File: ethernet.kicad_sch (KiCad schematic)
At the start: 45 parts, among them J401 Bus_RJ45_5-2337992-8, Q401 PJE138K, U401 TPS2372-3RGWR, U402 ACPL-217-500E, U403 ULS-12/5-D48N-C

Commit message: [#53901] Update symbols & footprints from lib
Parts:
- D404: footprint antmicro-footprints:LED_0603_1608Metric_R -> antmicro-footprints:LED_0603_1608Metric_G; symbol antmicroLEDIndicationDiscrete:LED_R_0603_598-8D80-107F -> antmicroLEDIndicationDiscrete:LED_G_0603_598-8D80-107F
- R407, R409, R410, R417, R419, R420, R422, R423: DNP DNP -> (none); now in the parts list
- U403: value ULS-12/5-D48N-C -> ULS-12_5-D48N-C; symbol antmicroDCDCConverters:ULS-12/5-D48N-C -> antmicroDCDCConverters:ULS-12_5-D48N-C

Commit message: [#56708] Add loclib
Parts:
- C401: footprint antmicro-footprints:C_0805_2012Metric -> cm4-baseboard-footprints:C_0805_2012Metric; symbol antmicroCapacitorsmisc:C_100n_100V_0805 -> cm4-baseboard:C_100n_100V_0805
- C402: footprint antmicro-footprints:C_0402_1005Metric -> cm4-baseboard-footprints:C_0402_1005Metric; symbol antmicroCapacitors0402:C_10n_0402 -> cm4-baseboard:C_10n_0402
- C403, C411: footprint antmicro-footprints:C_0402_1005Metric -> cm4-baseboard-footprints:C_0402_1005Metric; symbol antmicroCapacitors0402:C_100n_0402 -> cm4-baseboard:C_100n_0402
- C404, C405, C406, C407: footprint antmicro-footprints:C_2220_5650Metric -> cm4-baseboard-footprints:C_2220_5650Metric; symbol antmicroCapacitorsmisc:C_22u_100V_2220 -> cm4-baseboard:C_22u_100V_2220
- C408, C409, C410: footprint antmicro-footprints:C_0805_2012Metric -> cm4-baseboard-footprints:C_0805_2012Metric; symbol antmicroCapacitorsmisc:C_22u_25V_0805 -> cm4-baseboard:C_22u_25V_0805
- D401, D402: footprint antmicro-footprints:DFN3538 -> cm4-baseboard-footprints:DFN3538; symbol antmicroTVSDiodes:CD-MMBL110S -> cm4-baseboard:CD-MMBL110S
- D403: footprint antmicro-footprints:D_SOD-123F -> cm4-baseboard-footprints:D_SOD-123F; symbol antmicroDiodesRectifiersSingle:PTVS58VS1UR,115 -> cm4-baseboard:PTVS58VS1UR,115
- D404: footprint antmicro-footprints:LED_0603_1608Metric_G -> cm4-baseboard-footprints:LED_0603_1608Metric_G; symbol antmicroLEDIndicationDiscrete:LED_G_0603_598-8D80-107F -> cm4-baseboard:LED_G_0603_598-8D80-107F
- FB401, FB402: footprint antmicro-footprints:FB_0603_1608Metric -> cm4-baseboard-footprints:FB_0603_1608Metric; symbol antmicroFerriteBeadsandChips:FB_220Z_2.2A_TDK-MPZ_0603 -> cm4-baseboard:FB_220Z_2.2A_TDK-MPZ_0603
- J401: footprint antmicro-footprints:RJ45_5-2337992-8_Horizontal -> cm4-baseboard-footprints:RJ45_5-2337992-8_Horizontal; symbol antmicroModularConnectorsJacksWithMagnetics:Bus_RJ45_5-2337992-8 -> cm4-baseboard:Bus_RJ45_5-2337992-8
- Q401: footprint antmicro-footprints:SOT-523 -> cm4-baseboard-footprints:SOT-523; symbol antmicroTransistorsFETsMOSFETsSingle:PJE138K -> cm4-baseboard:PJE138K
- R401: footprint antmicro-footprints:R_0402_1005Metric -> cm4-baseboard-footprints:R_0402_1005Metric; symbol antmicroResistors0402:R_1k3_0402 -> cm4-baseboard:R_1k3_0402
- R402: footprint antmicro-footprints:R_0402_1005Metric -> cm4-baseboard-footprints:R_0402_1005Metric; symbol antmicroResistors0402:R_49k9_0402 -> cm4-baseboard:R_49k9_0402
- R403, R417, R422, R423: footprint antmicro-footprints:R_0402_1005Metric -> cm4-baseboard-footprints:R_0402_1005Metric; symbol antmicroResistors0402:R_0R_0402 -> cm4-baseboard:R_0R_0402
- R404: footprint antmicro-footprints:R_0603_1608Metric -> cm4-baseboard-footprints:R_0603_1608Metric; symbol antmicroResistors0603:R_63R4_0603 -> cm4-baseboard:R_63R4_0603
- R405: footprint antmicro-footprints:R_0402_1005Metric -> cm4-baseboard-footprints:R_0402_1005Metric; symbol antmicroResistors0402:R_1k2_0402 -> cm4-baseboard:R_1k2_0402
- R406, R414: footprint antmicro-footprints:R_0402_1005Metric -> cm4-baseboard-footprints:R_0402_1005Metric; symbol antmicroResistors0402:R_24k9_0402 -> cm4-baseboard:R_24k9_0402
- R407, R408, R409, R410: footprint antmicro-footprints:R_0402_1005Metric -> cm4-baseboard-footprints:R_0402_1005Metric; symbol antmicroResistors0402:R_10k_0402 -> cm4-baseboard:R_10k_0402
- R411, R412, R413: footprint antmicro-footprints:R_0402_1005Metric -> cm4-baseboard-footprints:R_0402_1005Metric; symbol antmicroResistors0402:R_200R_0402 -> cm4-baseboard:R_200R_0402
- R415, R419: footprint antmicro-footprints:R_0402_1005Metric -> cm4-baseboard-footprints:R_0402_1005Metric; symbol antmicroResistors0402:R_470k_0402 -> cm4-baseboard:R_470k_0402
- R416, R420: footprint antmicro-footprints:R_0402_1005Metric -> cm4-baseboard-footprints:R_0402_1005Metric; symbol antmicroResistors0402:R_100k_0402 -> cm4-baseboard:R_100k_0402
- R418, R421: footprint antmicro-footprints:R_0402_1005Metric -> cm4-baseboard-footprints:R_0402_1005Metric; symbol antmicroResistors0402:R_1k_0402 -> cm4-baseboard:R_1k_0402
- U401: footprint antmicro-footprints:VQFN-20_5x5x1mm_P0.65mm -> cm4-baseboard-footprints:VQFN-20_5x5x1mm_P0.65mm; symbol antmicroPMICPowerDistributionSwitchesLoadDrivers:TPS2372-3RGWR -> cm4-baseboard:TPS2372-3RGWR
- U402: footprint antmicro-footprints:SOIC-4_4.55x2.6mm_P1.27mm -> cm4-baseboard-footprints:SOIC-4_4.55x2.6mm_P1.27mm; symbol antmicroOptoisolatorsLogicOutput:ACPL-217-500E -> cm4-baseboard:ACPL-217-500E
- U403: footprint antmicro-footprints:ULS-12_5-D48N-C -> cm4-baseboard-footprints:ULS-12_5-D48N-C; symbol antmicroDCDCConverters:ULS-12_5-D48N-C -> cm4-baseboard:ULS-12_5-D48N-C

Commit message: [#56708] Update symbol/footprint props; Update modules visibilty
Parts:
- D404: value LED_G -> LED_G_0603_598-8D80-107F; Color (none) -> Green
- R407, R409, R410, R417, R419, R420, R422, R423: DNP (none) -> DNP; now left out of the parts list
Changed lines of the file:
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@@
   )
   (symbol (lib_id "cm4-baseboard:R_0R_0402") (at 331.47 191.77 270) (unit 1)
-    (in_bom yes) (on_board yes) (dnp yes)
+    (in_bom no) (on_board yes) (dnp yes)
     (property "Reference" "R423" (at 332.74 193.04 90)
       (effects (font (size 1.27 1.27)) (justify left))
@@
     (property "Current" "1A" (at 330.2 191.135 0)
       (effects (font (size 1.27 1.27) (thickness 0.15)) hide)
+    )
+    (property "DNP" "DNP" (at 331.47 194.31 0)
+      (effects (font (size 1 1)))
     )
     (pin "1")
@@
   )
   (symbol (lib_id "cm4-baseboard:R_0R_0402") (at 274.32 194.31 180) (unit 1)
-    (in_bom yes) (on_board yes) (dnp yes)
+    (in_bom no) (on_board yes) (dnp yes)
     (property "Reference" "R417" (at 271.78 190.5 0)
       (effects (font (size 1.27 1.27)))
@@
       (effects (font (size 1.27 1.27) (thickness 0.15)) hide)
     )
+    (property "DNP" "DNP" (at 271.78 194.31 0)
+      (effects (font (size 1 1)))
+    )
     (pin "1")
     (pin "2")
@@
       (effects (font (size 1.27 1.27) (thickness 0.15)) (justify left))
     )
-    (property "Value" "LED_G" (at 252.73 198.4375 90)
-      (effects (font (size 1.27 1.27) (thickness 0.15)) (justify left))
-    )
-    (property "Footprint" "cm4-baseboard-footprints:LED_0603_1608Metric_G" (at 240.03 215.9 0)
-      (effects (font (size 1.27 1.27) (thickness 0.15)) (justify left bottom) hide)
-    )
-    (property "Datasheet" "https://www.farnell.com/datasheets/3093797.pdf" (at 237.49 215.9 0)
-      (effects (font (size 1.27 1.27) (thickness 0.15)) (justify left bottom) hide)
-    )
-    (property "MPN" "598-8D80-107F" (at 234.95 215.9 0)
-      (effects (font (size 1.27 1.27) (thickness 0.15)) (justify left bottom) hide)
-    )
-    (property "Manufacturer" "Dialight" (at 232.41 215.9 0)
-      (effects (font (size 1.27 1.27) (thickness 0.15)) (justify left bottom) hide)
-    )
-    (property "Author" "Antmicro" (at 229.87 215.9 0)
-      (effects (font (size 1.27 1.27) (thickness 0.15)) (justify left bottom) hide)
-    )
-    (property "License" "Apache-2.0" (at 227.33 215.9 0)
-      (effects (font (size 1.27 1.27) (thickness 0.15)) (justify left bottom) hide)
+    (property "Value" "LED_G_0603_598-8D80-107F" (at 240.03 215.9 0)
+      (effects (font (size 1.27 1.27) (thickness 0.15)) (justify left bottom) hide)
+    )
+    (property "Footprint" "cm4-baseboard-footprints:LED_0603_1608Metric_G" (at 237.49 215.9 0)
+      (effects (font (size 1.27 1.27) (thickness 0.15)) (justify left bottom) hide)
+    )
+    (property "Datasheet" "https://www.farnell.com/datasheets/3093797.pdf" (at 234.95 215.9 0)
+      (effects (font (size 1.27 1.27) (thickness 0.15)) (justify left bottom) hide)
+    )
+    (property "MPN" "598-8D80-107F" (at 232.41 215.9 0)
+      (effects (font (size 1.27 1.27) (thickness 0.15)) (justify left bottom) hide)
+    )
+    (property "Manufacturer" "Dialight" (at 229.87 215.9 0)
+      (effects (font (size 1.27 1.27) (thickness 0.15)) (justify left bottom) hide)
+    )
+    (property "Author" "Antmicro" (at 227.33 215.9 0)
+      (effects (font (size 1.27 1.27) (thickness 0.15)) (justify left bottom) hide)
+    )
+    (property "License" "Apache-2.0" (at 224.79 215.9 0)
+      (effects (font (size 1.27 1.27) (thickness 0.15)) (justify left bottom) hide)
+    )
+    (property "Color" "Green" (at 252.73 198.4375 90)
+      (effects (font (size 1.27 1.27)) (justify left))
     )
     (pin "1")
@@
   (symbol (lib_id "cm4-baseboard:FB_220Z_2.2A_TDK-MPZ_0603") (at 97.79 213.36 0) (unit 1)
     (in_bom yes) (on_board yes) (dnp no) (fields_autoplaced)
-    (property "Reference" "FB402" (at 100.2919 217.17 0)
+    (property "Reference" "FB402" (at 100.2919 207.01 0)
       (effects (font (size 1.27 1.27)))
     )
@@
       (effects (font (size 1.27 1.27) (thickness 0.15)) (justify left bottom) hide)
     )
-    (property "Val" "220Z/2.2A" (at 0 426.72 0)
+    (property "Val" "220Z/2.2A" (at 100.2919 209.55 0)
       (effects (font (size 1.27 1.27)))
     )
@@
   )
   (symbol (lib_id "cm4-baseboard:R_470k_0402") (at 287.02 189.23 90) (unit 1)
-    (in_bom yes) (on_board yes) (dnp yes)
+    (in_bom no) (on_board yes) (dnp yes)
     (property "Reference" "R419" (at 288.29 185.42 90)
       (effects (font (size 1.27 1.27)) (justify right))
@@
       (effects (font (size 1.27 1.27)) (justify left bottom) hide)
     )
+    (property "DNP" "DNP" (at 287.02 186.69 0)
+      (effects (font (size 1 1)))
+    )
     (pin "1")
     (pin "2")
@@
   )
   (symbol (lib_id "cm4-baseboard:R_100k_0402") (at 287.02 203.2 90) (unit 1)
-    (in_bom yes) (on_board yes) (dnp yes)
+    (in_bom no) (on_board yes) (dnp yes)
     (property "Reference" "R420" (at 288.29 199.39 90)
       (effects (font (size 1.27 1.27)) (justify right))
@@
       (effects (font (size 1.27 1.27)) (justify left bottom) hide)
     )
+    (property "DNP" "DNP" (at 287.02 200.66 0)
+      (effects (font (size 1 1)))
+    )
     (pin "1")
     (pin "2")
@@
   )
   (symbol (lib_id "cm4-baseboard:R_0R_0402") (at 331.47 184.15 270) (unit 1)
-    (in_bom yes) (on_board yes) (dnp yes)
+    (in_bom no) (on_board yes) (dnp yes)
     (property "Reference" "R422" (at 332.74 185.42 90)
       (effects (font (size 1.27 1.27)) (justify left))
@@
     (property "Current" "1A" (at 330.2 183.515 0)
       (effects (font (size 1.27 1.27) (thickness 0.15)) hide)
+    )
+    (property "DNP" "DNP" (at 331.47 186.69 0)
+      (effects (font (size 1 1)))
     )
     (pin "1")
@@
   )
   (symbol (lib_id "cm4-baseboard:R_10k_0402") (at 185.42 189.23 90) (unit 1)
-    (in_bom yes) (on_board yes) (dnp yes) (fields_autoplaced)
+    (in_bom no) (on_board yes) (dnp yes)
     (property "Reference" "R407" (at 186.69 186.055 90)
       (effects (font (size 1.27 1.27)) (justify right))
@@
       (effects (font (size 1.27 1.27)) (justify left bottom) hide)
     )
+    (property "DNP" "DNP" (at 185.42 186.69 0)
+      (effects (font (size 1 1)))
+    )
     (pin "1")
     (pin "2")
@@
       (effects (font (size 1.27 1.27) (thickness 0.15)) (justify left bottom) hide)
     )
-    (property "Val" "220Z/2.2A" (at 0 365.76 0)
+    (property "Val" "220Z/2.2A" (at 100.2919 179.07 0)
       (effects (font (size 1.27 1.27)))
     )
@@
   )
   (symbol (lib_id "cm4-baseboard:R_10k_0402") (at 195.58 189.23 90) (unit 1)
-    (in_bom yes) (on_board yes) (dnp yes)
+    (in_bom no) (on_board yes) (dnp yes)
     (property "Reference" "R409" (at 196.85 186.055 90)
       (effects (font (size 1.27 1.27)) (justify right))
@@
       (effects (font (size 1.27 1.27)) (justify left bottom) hide)
     )
+    (property "DNP" "DNP" (at 195.58 186.69 0)
+      (effects (font (size 1 1)))
+    )
     (pin "1")
     (pin "2")
@@
   )
   (symbol (lib_id "cm4-baseboard:R_10k_0402") (at 204.47 189.23 90) (unit 1)
-    (in_bom yes) (on_board yes) (dnp yes)
+    (in_bom no) (on_board yes) (dnp yes)
     (property "Reference" "R410" (at 205.74 186.055 90)
       (effects (font (size 1.27 1.27)) (justify right))
@@
       (effects (font (size 1.27 1.27)) (justify left bottom) hide)
     )
-    (pin "1")
+    (property "DNP" "DNP" (at 204.47 186.69 0)
+      (effects (font (size 1 1)))
+    )
+    (pin "1")

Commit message: [#57456] Remove loclib
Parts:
- C401: footprint cm4-baseboard-footprints:C_0805_2012Metric -> antmicro-footprints:C_0805_2012Metric; symbol cm4-baseboard:C_100n_100V_0805 -> antmicroCapacitorsmisc:C_100n_100V_0805
- C402: footprint cm4-baseboard-footprints:C_0402_1005Metric -> antmicro-footprints:C_0402_1005Metric; symbol cm4-baseboard:C_10n_0402 -> antmicroCapacitors0402:C_10n_0402
- C403, C411: footprint cm4-baseboard-footprints:C_0402_1005Metric -> antmicro-footprints:C_0402_1005Metric; symbol cm4-baseboard:C_100n_0402 -> antmicroCapacitors0402:C_100n_0402
- C404, C405, C406, C407: footprint cm4-baseboard-footprints:C_2220_5650Metric -> antmicro-footprints:C_2220_5650Metric; symbol cm4-baseboard:C_22u_100V_2220 -> antmicroCapacitorsmisc:C_22u_100V_2220
- C408, C409, C410: footprint cm4-baseboard-footprints:C_0805_2012Metric -> antmicro-footprints:C_0805_2012Metric; symbol cm4-baseboard:C_22u_25V_0805 -> antmicroCapacitorsmisc:C_22u_25V_0805
- D401, D402: footprint cm4-baseboard-footprints:DFN3538 -> antmicro-footprints:DFN3538; symbol cm4-baseboard:CD-MMBL110S -> antmicroTVSDiodes:CD-MMBL110S
- D403: footprint cm4-baseboard-footprints:D_SOD-123F -> antmicro-footprints:D_SOD-123F; symbol cm4-baseboard:PTVS58VS1UR,115 -> antmicroDiodesRectifiersSingle:PTVS58VS1UR,115
- D404: footprint cm4-baseboard-footprints:LED_0603_1608Metric_G -> antmicro-footprints:LED_0603_1608Metric_G; symbol cm4-baseboard:LED_G_0603_598-8D80-107F -> antmicroLEDIndicationDiscrete:LED_G_0603_598-8D80-107F
- FB401, FB402: footprint cm4-baseboard-footprints:FB_0603_1608Metric -> antmicro-footprints:FB_0603_1608Metric; symbol cm4-baseboard:FB_220Z_2.2A_TDK-MPZ_0603 -> antmicroFerriteBeadsandChips:FB_220Z_2.2A_TDK-MPZ_0603
- J401: footprint cm4-baseboard-footprints:RJ45_5-2337992-8_Horizontal -> antmicro-footprints:RJ45_X-2337992-8_Horizontal; symbol cm4-baseboard:Bus_RJ45_5-2337992-8 -> antmicroModularConnectorsJacksWithMagnetics:Bus_RJ45_5-2337992-8
- Q401: footprint cm4-baseboard-footprints:SOT-523 -> antmicro-footprints:SOT-523; symbol cm4-baseboard:PJE138K -> antmicroTransistorsFETsMOSFETsSingle:PJE138K
- R401: footprint cm4-baseboard-footprints:R_0402_1005Metric -> antmicro-footprints:R_0402_1005Metric; symbol cm4-baseboard:R_1k3_0402 -> antmicroResistors0402:R_1k3_0402
- R402: footprint cm4-baseboard-footprints:R_0402_1005Metric -> antmicro-footprints:R_0402_1005Metric; symbol cm4-baseboard:R_49k9_0402 -> antmicroResistors0402:R_49k9_0402
- R403, R417, R422, R423: footprint cm4-baseboard-footprints:R_0402_1005Metric -> antmicro-footprints:R_0402_1005Metric; symbol cm4-baseboard:R_0R_0402 -> antmicroResistors0402:R_0R_0402
- R404: footprint cm4-baseboard-footprints:R_0603_1608Metric -> antmicro-footprints:R_0603_1608Metric; symbol cm4-baseboard:R_63R4_0603 -> antmicroResistors0603:R_63R4_0603
- R405: footprint cm4-baseboard-footprints:R_0402_1005Metric -> antmicro-footprints:R_0402_1005Metric; symbol cm4-baseboard:R_1k2_0402 -> antmicroResistors0402:R_1k2_0402
- R406, R414: footprint cm4-baseboard-footprints:R_0402_1005Metric -> antmicro-footprints:R_0402_1005Metric; symbol cm4-baseboard:R_24k9_0402 -> antmicroResistors0402:R_24k9_0402
- R407, R408, R409, R410: footprint cm4-baseboard-footprints:R_0402_1005Metric -> antmicro-footprints:R_0402_1005Metric; symbol cm4-baseboard:R_10k_0402 -> antmicroResistors0402:R_10k_0402
- R411, R412, R413: footprint cm4-baseboard-footprints:R_0402_1005Metric -> antmicro-footprints:R_0402_1005Metric; symbol cm4-baseboard:R_200R_0402 -> antmicroResistors0402:R_200R_0402
- R415, R419: footprint cm4-baseboard-footprints:R_0402_1005Metric -> antmicro-footprints:R_0402_1005Metric; symbol cm4-baseboard:R_470k_0402 -> antmicroResistors0402:R_470k_0402
- R416, R420: footprint cm4-baseboard-footprints:R_0402_1005Metric -> antmicro-footprints:R_0402_1005Metric; symbol cm4-baseboard:R_100k_0402 -> antmicroResistors0402:R_100k_0402
- R418, R421: footprint cm4-baseboard-footprints:R_0402_1005Metric -> antmicro-footprints:R_0402_1005Metric; symbol cm4-baseboard:R_1k_0402 -> antmicroResistors0402:R_1k_0402
- U401: footprint cm4-baseboard-footprints:VQFN-20_5x5x1mm_P0.65mm -> antmicro-footprints:VQFN-20_5x5x1mm_P0.65mm; symbol cm4-baseboard:TPS2372-3RGWR -> antmicroPMICPowerDistributionSwitchesLoadDrivers:TPS2372-3RGWR
- U402: footprint cm4-baseboard-footprints:SOIC-4_4.55x2.6mm_P1.27mm -> antmicro-footprints:SOIC-4_4.55x2.6mm_P1.27mm; symbol cm4-baseboard:ACPL-217-500E -> antmicroOptoisolatorsLogicOutput:ACPL-217-500E
- U403: footprint cm4-baseboard-footprints:ULS-12_5-D48N-C -> antmicro-footprints:ULS-12_5-D48N-C; symbol cm4-baseboard:ULS-12_5-D48N-C -> antmicroDCDCConverters:ULS-12_5-D48N-C

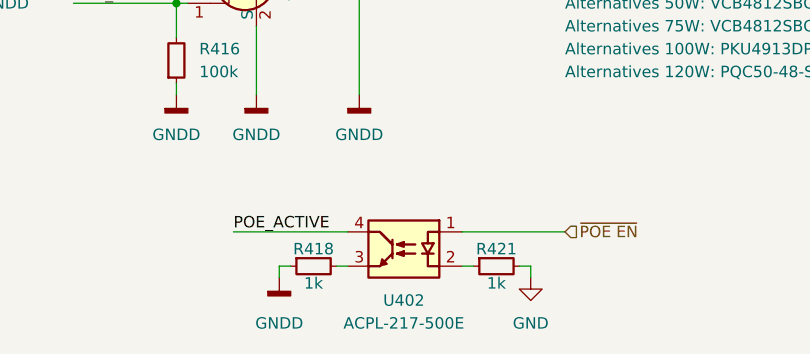
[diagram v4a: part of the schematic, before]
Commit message: [#58122] LED related fixes & improvements
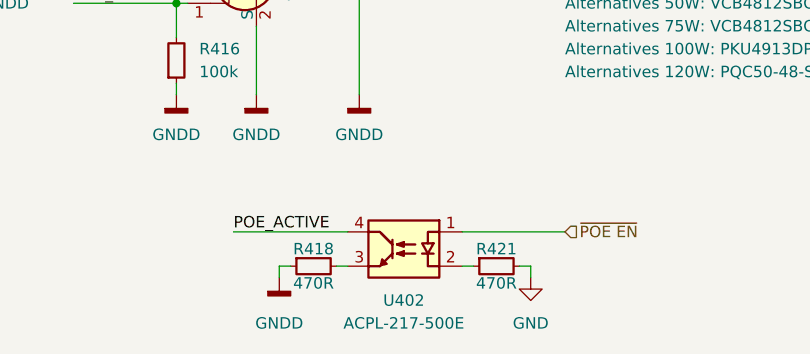
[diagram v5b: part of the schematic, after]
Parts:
- R418, R421: value R_1k_0402 -> R_470R_0402; symbol antmicroResistors0402:R_1k_0402 -> antmicroResistors0402:R_470R_0402; MPN CR0402-FX-1001GLF -> CR0402-FX-4700GLF; Val 1k -> 470R
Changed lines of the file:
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@@
     )
   )
-  (symbol (lib_id "antmicroResistors0402:R_1k_0402") (at 279.4 236.22 0) (unit 1)
+  (symbol (lib_id "antmicroResistors0402:R_470R_0402") (at 279.4 236.22 0) (unit 1)
     (in_bom yes) (on_board yes) (dnp no)
     (property "Reference" "R418" (at 281.94 234.315 0)
       (effects (font (size 1.27 1.27)))
     )
-    (property "Value" "R_1k_0402" (at 299.72 248.92 0)
+    (property "Value" "R_470R_0402" (at 299.72 248.92 0)
       (effects (font (size 1.27 1.27) (thickness 0.15)) (justify left bottom) hide)
     )
@@
       (effects (font (size 1.27 1.27) (thickness 0.15)) (justify left bottom) hide)
     )
-    (property "MPN" "CR0402-FX-1001GLF" (at 299.72 256.54 0)
-      (effects (font (size 1.27 1.27) (thickness 0.15)) (justify left bottom) hide)
-    )
-    (property "Val" "1k" (at 281.94 238.125 0)
+    (property "MPN" "CR0402-FX-4700GLF" (at 299.72 256.54 0)
+      (effects (font (size 1.27 1.27) (thickness 0.15)) (justify left bottom) hide)
+    )
+    (property "Val" "470R" (at 281.94 238.125 0)
       (effects (font (size 1.27 1.27) (thickness 0.15)))
     )
@@
     )
   )
-  (symbol (lib_id "antmicroResistors0402:R_1k_0402") (at 299.72 236.22 0) (unit 1)
+  (symbol (lib_id "antmicroResistors0402:R_470R_0402") (at 299.72 236.22 0) (unit 1)
     (in_bom yes) (on_board yes) (dnp no)
     (property "Reference" "R421" (at 302.26 234.315 0)
       (effects (font (size 1.27 1.27)))
     )
-    (property "Value" "R_1k_0402" (at 320.04 248.92 0)
+    (property "Value" "R_470R_0402" (at 320.04 248.92 0)
       (effects (font (size 1.27 1.27) (thickness 0.15)) (justify left bottom) hide)
     )
@@
       (effects (font (size 1.27 1.27) (thickness 0.15)) (justify left bottom) hide)
     )
-    (property "MPN" "CR0402-FX-1001GLF" (at 320.04 256.54 0)
-      (effects (font (size 1.27 1.27) (thickness 0.15)) (justify left bottom) hide)
-    )
-    (property "Val" "1k" (at 302.26 238.125 0)
+    (property "MPN" "CR0402-FX-4700GLF" (at 320.04 256.54 0)
+      (effects (font (size 1.27 1.27) (thickness 0.15)) (justify left bottom) hide)
+    )
+    (property "Val" "470R" (at 302.26 238.125 0)
       (effects (font (size 1.27 1.27) (thickness 0.15)))
     )
